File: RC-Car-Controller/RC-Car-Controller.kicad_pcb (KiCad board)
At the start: 2 copper layers, 138 x 77 mm, 70 parts, among them J1 Conn_01x02, J3 Conn_01x08_Pin, J5 MCU_IF, J6 ANT_IF, J7 2171790001, Q1 DMG2301L, SW1 SW_Push, SW2 1825027-8, SW4 1825027-8, U1 TPS62132, U10 STC3100IST, U2 USBLC6-2SC6, U4 STM32H743VGTx, U8 BQ25303JRTER, Y1 Crystal

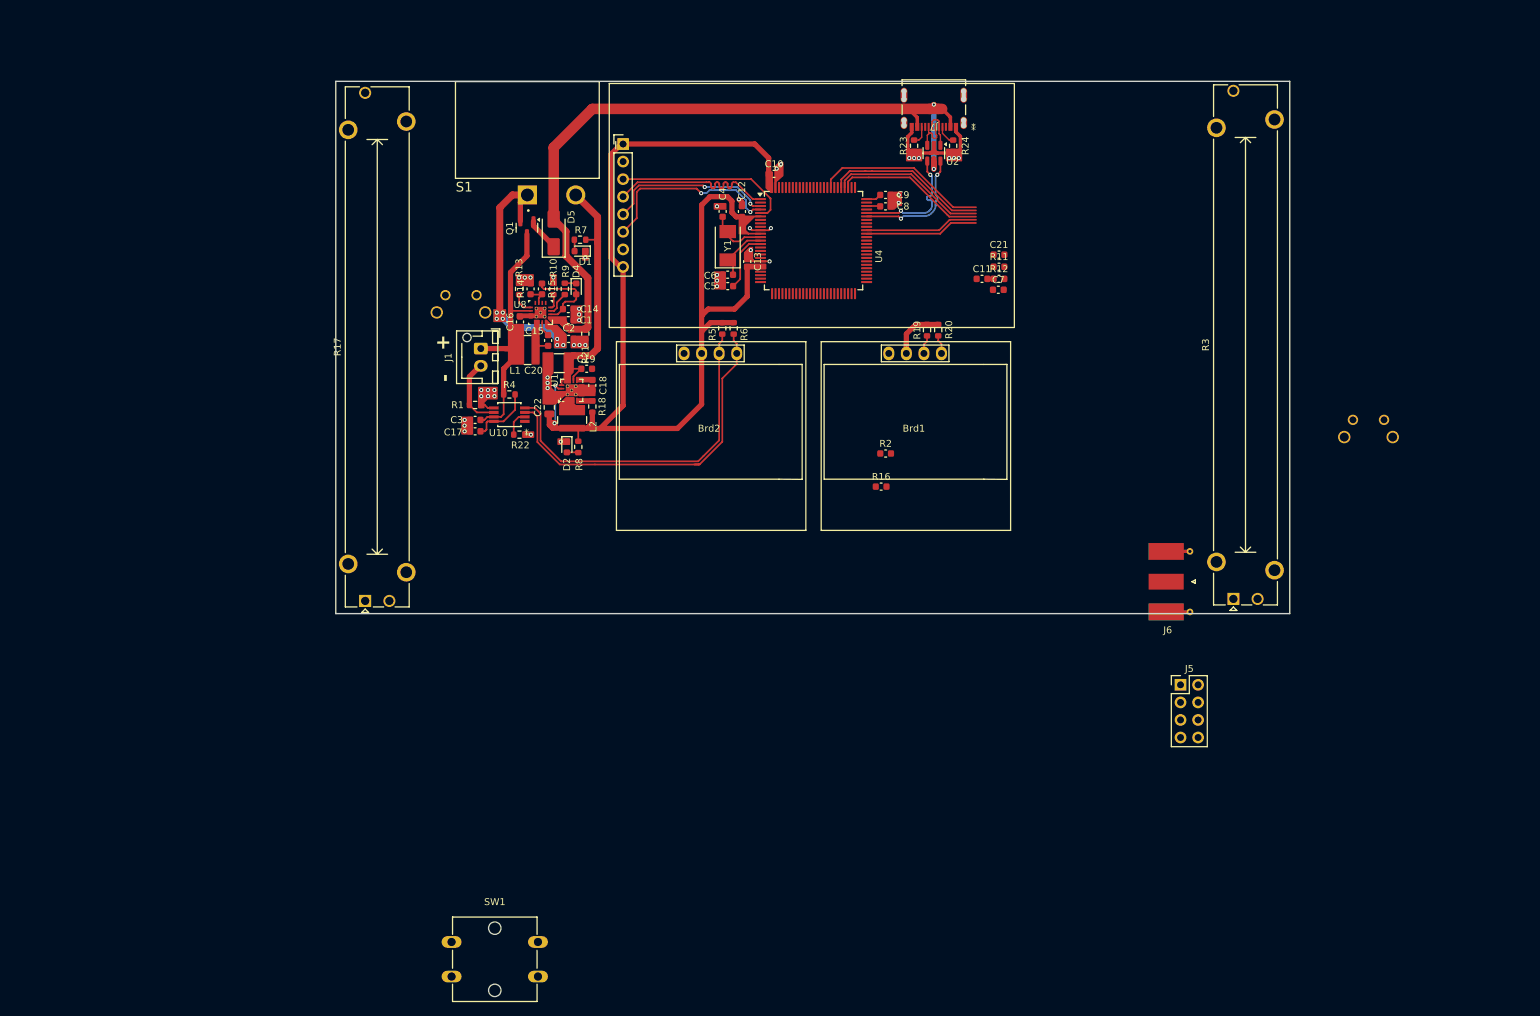
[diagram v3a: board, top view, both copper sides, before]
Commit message: Finished non-RF Controller PCB
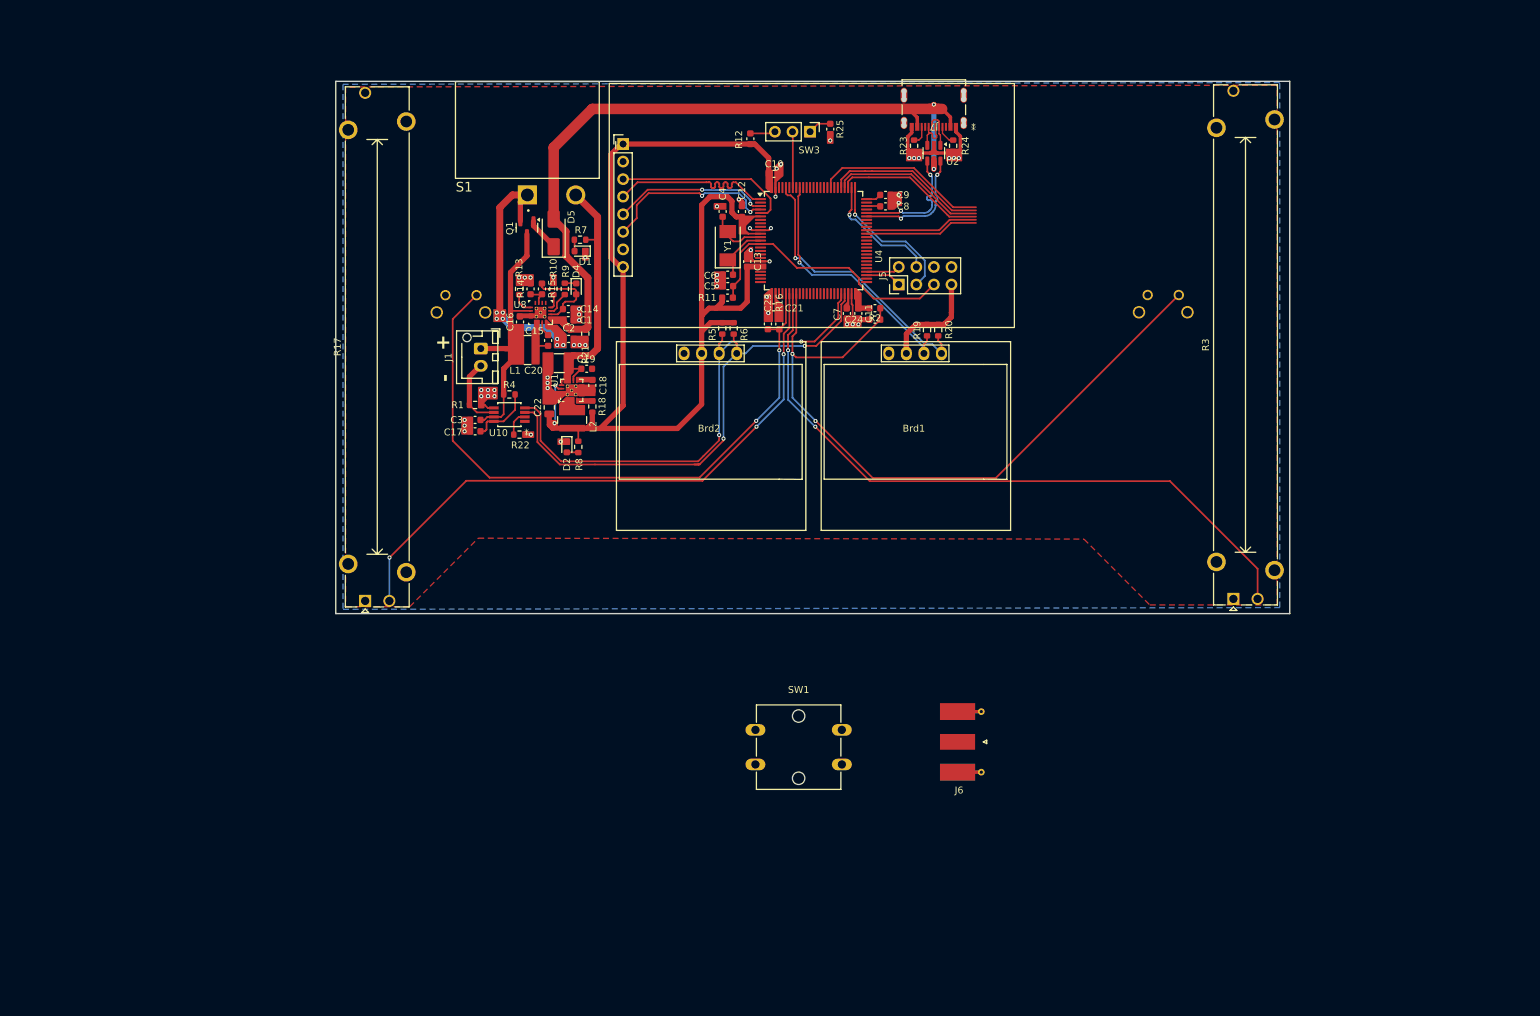
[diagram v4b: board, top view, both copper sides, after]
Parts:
- added C23: 0.22uF/10V, Capacitor_SMD:C_0603_1608Metric, F.Cu at (143.5, 78.1)
- added C24: 0.22uF/10V, Capacitor_SMD:C_0603_1608Metric, F.Cu at (159.0, 77.5)
- added R25: 10k, Capacitor_SMD:C_0603_1608Metric, F.Cu at (152.5, 49.9)
- added SW3: SW_SPDT, Connector_PinHeader_2.54mm:PinHeader_1x03_P2.54mm_Vertical, F.Cu at (149.6, 50.3)
- moved J5 70.8 mm to (162.4, 72.4), turned to 90 degrees
- moved SW1 53.6 mm to (141.7, 136.8)
- moved R12 41.3 mm to (141.0, 51.3), turned to -90 degrees
- moved R11 39.5 mm to (137.7, 74.3)
- moved J6 38.1 mm to (172.7, 138.6)
- moved SW2 34.8 mm to (198.4, 73.9)
- moved C21 33.5 mm to (144.3, 75.7), turned to 180 degrees
- moved R16 27.8 mm to (145.2, 78.1), turned to 90 degrees
- moved C7 22.2 mm to (154.9, 76.6), turned to -90 degrees
- moved R2 21.1 mm to (159.0, 75.8), turned to 180 degrees
- moved C11 18.6 mm to (156.6, 76.6), turned to -90 degrees
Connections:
- Brd1 pad 3: /MCU/I2C2_SCL -> /MCU/I2C1_SCL
- Brd1 pad 4: /MCU/I2C2_SDA -> /MCU/I2C1_SDA
- Brd2 pad 3: /MCU/I2C1_SCL -> /MCU/I2C2_SCL
- Brd2 pad 4: /MCU/I2C1_SDA -> /MCU/I2C2_SDA
- R12 pad 1: unconnected-(R12-Pad1) -> Net-(SW3-C)
- R12 pad 2: GNDA -> +3V3
- R19 pad 1: /MCU/I2C2_SCL -> /MCU/I2C1_SCL
- R20 pad 1: /MCU/I2C2_SDA -> /MCU/I2C1_SDA
- R5 pad 1: /MCU/I2C1_SCL -> /MCU/I2C2_SCL
- R6 pad 1: /MCU/I2C1_SDA -> /MCU/I2C2_SDA
- U10 pad 3: /MCU/I2C1_SDA -> /MCU/I2C2_SDA
- U10 pad 4: /MCU/I2C1_SCL -> /MCU/I2C2_SCL
- U4 pad 30: unconnected-(U4-PA6-Pad30) -> /Inputs/Button_L
- U4 pad 31: unconnected-(U4-PA7-Pad31) -> /Inputs/Slider_L
- U4 pad 32: unconnected-(U4-PC4-Pad32) -> /Inputs/Slider_R
- U4 pad 33: unconnected-(U4-PC5-Pad33) -> /Inputs/Button_R
- U4 pad 76: unconnected-(U4-PA14-Pad76) -> /Connectors/SWCLK
- U4 pad 77: unconnected-(U4-PA15-Pad77) -> /Connectors/SWDIO
- U4 pad 94: unconnected-(U4-BOOT0-Pad94) -> Net-(SW3-B)
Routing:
- net /Inputs/Button_R: track 0.00 -> 103.8 mm, vias 0 -> 2
- net /Inputs/Slider_R: track 0.00 -> 98.0 mm, vias 0 -> 2
- net /Inputs/Button_L: track 0.00 -> 93.8 mm, vias 0 -> 2
- net /Inputs/Slider_L: track 0.00 -> 89.1 mm, vias 0 -> 3
- net /MCU/I2C2_SDA: track 2.74 -> 73.6 mm, vias 0 -> 2
- net /MCU/I2C2_SCL: track 2.73 -> 73.5 mm, vias 0 -> 2
- net /Connectors/NRST: track 8.71 -> 40.1 mm
- net /Connectors/SWCLK: track 0.00 -> 20.7 mm, vias 0 -> 1
- net /Connectors/SWDIO: track 0.00 -> 18.0 mm, vias 0 -> 1
- net /MCU/I2C1_SCL: track 50.4 -> 37.7 mm, vias 0 -> 1
- net /MCU/I2C1_SDA: track 52.4 -> 40.6 mm, vias 0 -> 1
- net +3V3: track 180.7 -> 191.7 mm
- net Net-(SW3-B): track 0.00 -> 8.09 mm
- net GNDA: track 24.9 -> 32.0 mm, vias 44 -> 51
- net /Connectors/USART_TX: track 0.00 -> 5.22 mm
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- added copper zone on F.Cu, net +3V3
- added copper zone on B.Cu, net GNDA

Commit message: Added FGH100M footprint/schematic
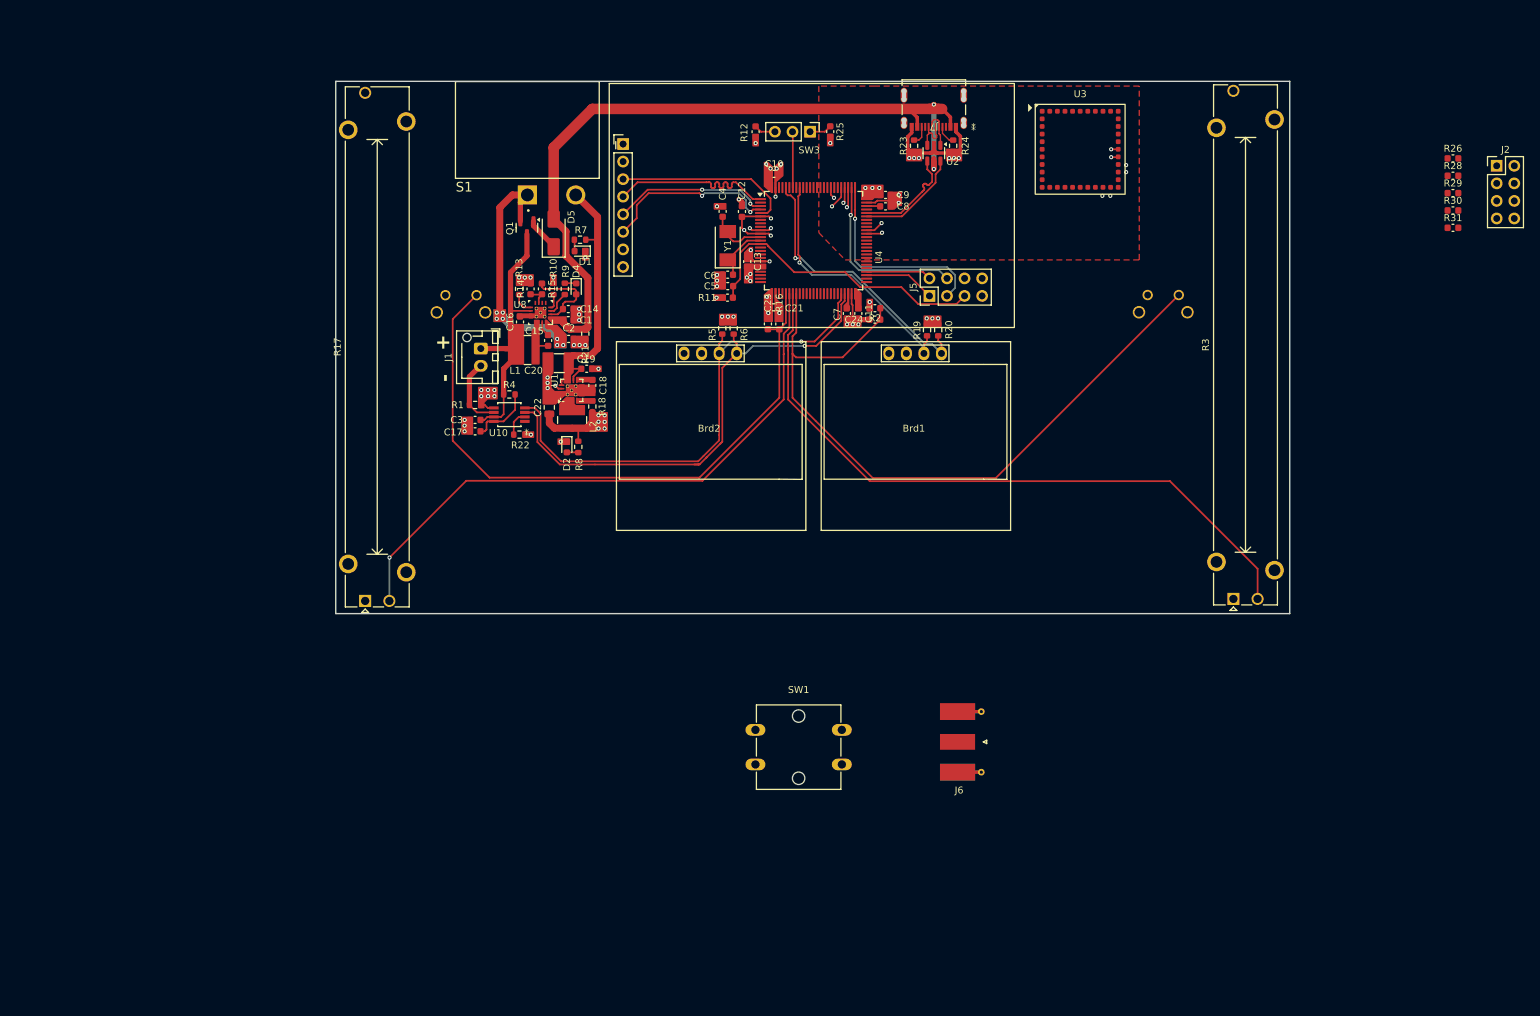
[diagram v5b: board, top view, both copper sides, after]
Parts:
- added J2: RF_IF, Connector_PinHeader_2.54mm:PinHeader_2x04_P2.54mm_Vertical, F.Cu at (248.9, 55.2)
- added R26: 10k, Capacitor_SMD:C_0603_1608Metric, F.Cu at (242.6, 54.1)
- added R28: 10k, Capacitor_SMD:C_0603_1608Metric, F.Cu at (242.6, 56.7)
- added R29: 10k, Capacitor_SMD:C_0603_1608Metric, F.Cu at (242.6, 59.2)
- added R30: 10k, Capacitor_SMD:C_0603_1608Metric, F.Cu at (242.6, 61.7)
- added R31: 10k, Capacitor_SMD:C_0603_1608Metric, F.Cu at (242.6, 64.2)
- added U3: ~, FGH100M:FGH100MABMD, F.Cu at (188.7, 52.8)
- moved J5 4.73 mm to (166.9, 74.0)
- moved R12 1.27 mm to (141.7, 50.3)
- moved R25 0.37 mm to (152.5, 50.3)
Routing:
- net +3V3: track 191.7 -> 23.2 mm, vias 2 -> 28
- net /MCU/SDMMC1_D1: track 16.4 -> 62.7 mm, vias 0 -> 2
- net /MCU/SDMMC1_D0: track 16.5 -> 62.6 mm, vias 0 -> 2
- net /MCU/SDMMC1_D2: track 22.0 -> 63.0 mm, vias 0 -> 2
- net /MCU/SDMMC1_D3: track 22.7 -> 63.1 mm, vias 0 -> 2
- net /MCU/SDMMC1_CK: track 23.5 -> 62.0 mm, vias 0 -> 2
- net /MCU/SDMMC1_CMD: track 25.2 -> 63.1 mm, vias 0 -> 2
- net /Connectors/SWCLK: track 20.7 -> 29.5 mm
- net /Connectors/SWDIO: track 18.0 -> 25.8 mm
- net /Connectors/USART_TX: track 5.22 -> 10.3 mm
- net /Connectors/USART_RX: track 4.94 -> 9.49 mm
- net GNDA: track 32.0 -> 36.1 mm, vias 51 -> 52
- net /Connectors/NRST: track 40.1 -> 44.0 mm
- net /Connectors/CON_USB_D+: track 18.0 -> 15.4 mm, vias 2 -> 0
- net /Connectors/CON_USB_D-: track 18.1 -> 15.4 mm, vias 2 -> 0
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- added copper zone on In2.Cu, net +3V3
- added copper zone on F.Cu, net GNDA
- added copper zone on In1.Cu, net GNDA
- removed copper zone on F.Cu, net +3V3
- removed copper zone on B.Cu, net GNDA
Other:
- copper layers 2 -> 4

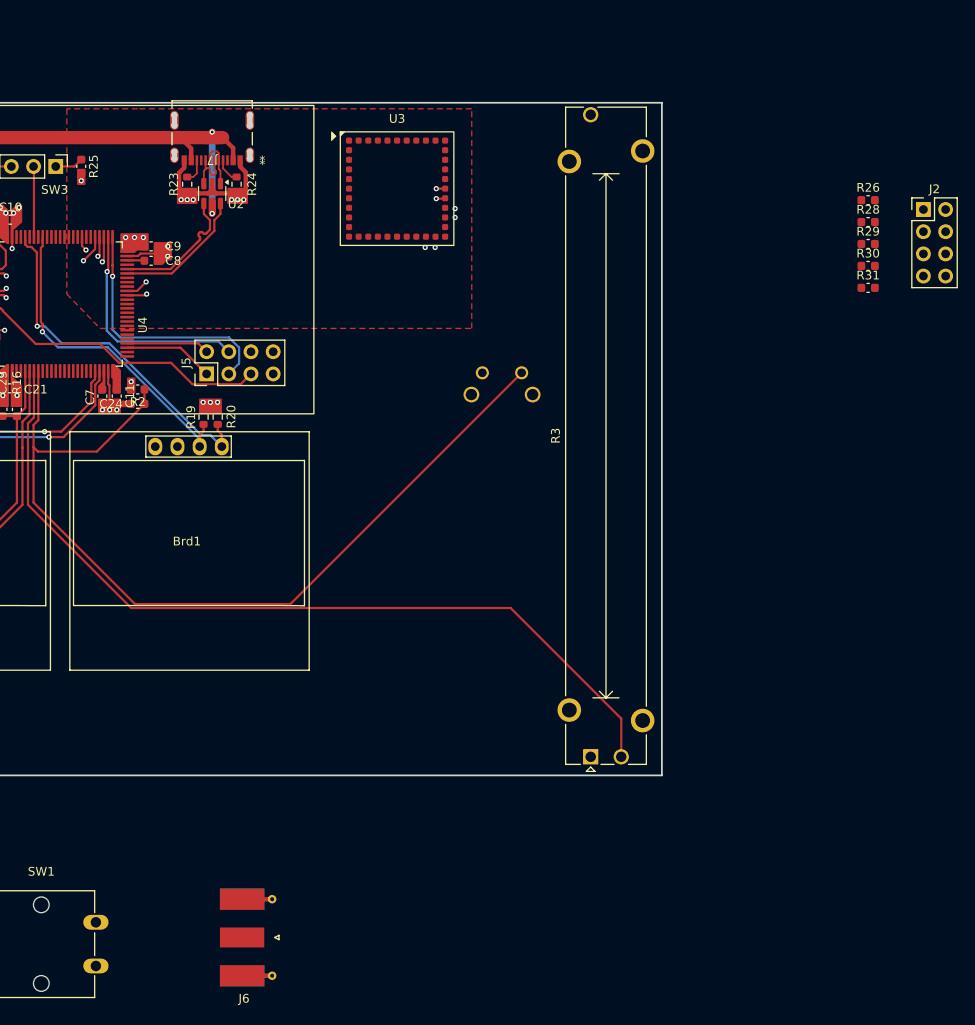
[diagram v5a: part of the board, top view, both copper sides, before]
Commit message: Wired up FGH100M
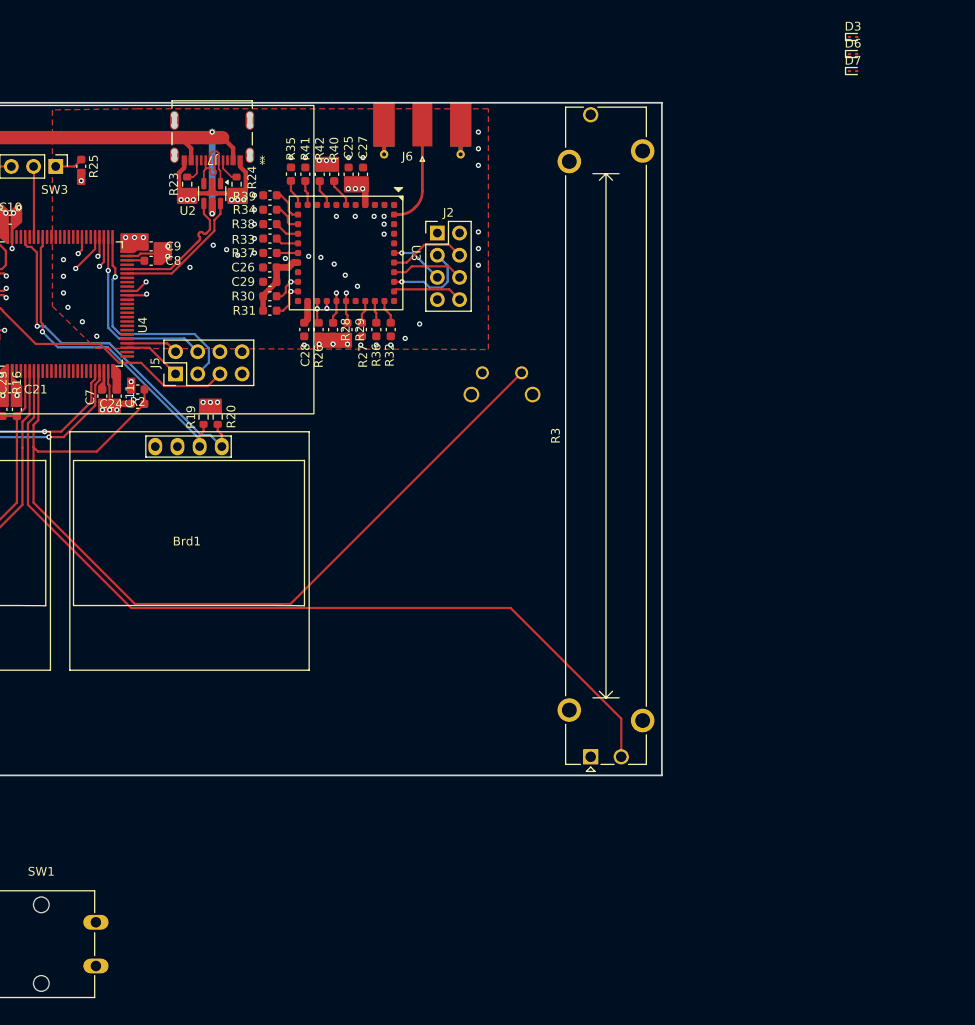
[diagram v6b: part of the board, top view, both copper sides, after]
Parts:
- added C25: 10uF/10V, Capacitor_SMD:C_0603_1608Metric, F.Cu at (183.1, 51.2)
- added C26: 10uF/10V, Capacitor_SMD:C_0603_1608Metric, F.Cu at (174.1, 61.8)
- added C27: 100nF/10V, Capacitor_SMD:C_0603_1608Metric, F.Cu at (184.8, 51.2)
- added C28: 100nF/10V, Capacitor_SMD:C_0603_1608Metric, F.Cu at (178.1, 69.0)
- added C29: 100nF/10V, Capacitor_SMD:C_0603_1608Metric, F.Cu at (174.1, 63.5)
- added D3: ESD9B5.0ST5G, Diode_SMD:D_SOD-923, F.Cu at (240.9, 35.5)
- added D6: ESD9B5.0ST5G, Diode_SMD:D_SOD-923, F.Cu at (240.9, 37.4)
- added D7: ESD9B5.0ST5G, Diode_SMD:D_SOD-923, F.Cu at (240.9, 39.4)
- added R27: 10k, Capacitor_SMD:C_0603_1608Metric, F.Cu at (184.7, 69.0)
- added R32: 10k, Capacitor_SMD:C_0603_1608Metric, F.Cu at (188.0, 69.0)
- added R33: 10k, Capacitor_SMD:C_0603_1608Metric, F.Cu at (174.1, 58.5)
- added R34: 10k, Capacitor_SMD:C_0603_1608Metric, F.Cu at (174.1, 55.2)
- added R35: 10k, Capacitor_SMD:C_0603_1608Metric, F.Cu at (176.5, 51.2)
- added R36: 10k, Capacitor_SMD:C_0603_1608Metric, F.Cu at (186.3, 69.0)
- added R37: 10k, Capacitor_SMD:C_0603_1608Metric, F.Cu at (174.1, 60.2)
- added R38: 10k, Capacitor_SMD:C_0603_1608Metric, F.Cu at (174.1, 56.9)
- added R39: 10k, Capacitor_SMD:C_0603_1608Metric, F.Cu at (174.1, 53.6)
- added R40: 10k, Capacitor_SMD:C_0603_1608Metric, F.Cu at (181.5, 51.2)
- added R41: 10k, Capacitor_SMD:C_0603_1608Metric, F.Cu at (178.2, 51.2)
- added R42: 10k, Capacitor_SMD:C_0603_1608Metric, F.Cu at (179.8, 51.2)
- moved J6 93.3 mm to (191.6, 47.2), turned to -90 degrees
- moved R30 68.6 mm to (174.1, 65.2), turned to 180 degrees
- moved R31 68.5 mm to (174.1, 66.8), turned to 180 degrees
- moved R26 64.6 mm to (179.7, 69.0), turned to -90 degrees
- moved R28 62.5 mm to (181.4, 69.0), turned to -90 degrees
- moved R29 60.4 mm to (183.0, 69.0), turned to -90 degrees
- moved J2 55.7 mm to (193.3, 57.9)
- moved U3 9.40 mm to (182.8, 60.2), turned to -90 degrees
- moved J5 3.56 mm to (163.3, 74.0)
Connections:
- J2 pad 8: /Connectors/RF_TDI -> /Connectors/RF_TDO
- U3 pad 10: unconnected-(U3-BUSY-Pad10) -> /MCU/RF_BUSY
- U3 pad 11: unconnected-(U3-GPIO1-Pad11) -> Net-(U3-GPIO1)
- U3 pad 12: unconnected-(U3-GPIO2-Pad12) -> Net-(U3-GPIO2)
- U3 pad 13: unconnected-(U3-GPIO3-Pad13) -> Net-(U3-GPIO3)
- U3 pad 14: unconnected-(U3-GPIO4-Pad14) -> Net-(U3-GPIO4)
- U3 pad 15: unconnected-(U3-GPIO5-Pad15) -> Net-(U3-GPIO5)
- U3 pad 16: unconnected-(U3-GPIO6-Pad16) -> Net-(U3-GPIO6)
- U3 pad 28: unconnected-(U3-GPIO9-Pad28) -> Net-(U3-GPIO9)
- U3 pad 29: unconnected-(U3-GPIO8-Pad29) -> Net-(U3-GPIO8)
- U3 pad 30: unconnected-(U3-GPIO7-Pad30) -> Net-(U3-GPIO7)
- U3 pad 32: unconnected-(U3-JTAG_TDO-Pad32) -> /Connectors/RF_TDO
- U3 pad 33: unconnected-(U3-JTAG_TMS-Pad33) -> /Connectors/RF_TMS
- U3 pad 34: unconnected-(U3-JTAG_TDI-Pad34) -> /Connectors/RF_TDI
- U3 pad 35: unconnected-(U3-JTAG_TRST-Pad35) -> /Connectors/RF_nTRST
- U3 pad 36: unconnected-(U3-JTAG_TCK-Pad36) -> /Connectors/RF_TCK
- U3 pad 40: unconnected-(U3-ANT_WIFI-Pad40) -> /Connectors/RF_ANT
- U3 pad 6: unconnected-(U3-WAKEUP_IN-Pad6) -> Net-(U3-WAKEUP_IN)
- U3 pad 8: unconnected-(U3-RESET_N-Pad8) -> /MCU/RF_RESET
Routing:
- net /MCU/SDMMC1_D2: track 63.0 -> 40.1 mm
- net /MCU/SDMMC1_D1: track 62.7 -> 39.9 mm
- net /MCU/SDMMC1_CK: track 62.0 -> 39.2 mm
- net /MCU/SDMMC1_CMD: track 63.1 -> 40.4 mm
- net /MCU/SDMMC1_D3: track 63.1 -> 40.7 mm
- net /MCU/SDMMC1_D0: track 62.6 -> 40.9 mm
- net +3V3: track 23.2 -> 37.0 mm, vias 28 -> 37
- net /Connectors/RF_ANT: track 0.00 -> 12.4 mm
- net /Connectors/RF_TMS: track 0.00 -> 10.2 mm, vias 0 -> 1
- net /Connectors/RF_nTRST: track 0.00 -> 8.82 mm
- net /Connectors/RF_TDI: track 0.00 -> 8.30 mm
- net /Connectors/RF_TDO: track 0.00 -> 8.08 mm
- net /Connectors/RF_TCK: track 0.00 -> 6.11 mm, vias 0 -> 1
- net /Connectors/SWDIO: track 25.8 -> 21.8 mm
- net Net-(U3-GPIO2): track 0.00 -> 3.87 mm
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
